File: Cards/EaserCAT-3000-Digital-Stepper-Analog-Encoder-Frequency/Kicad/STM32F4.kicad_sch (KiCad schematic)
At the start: 33 parts, among them J11 5V Power IN, J15 Serial usart1, J17 STLINK, U7 AMS1117-3.3, Y1 8 MHz

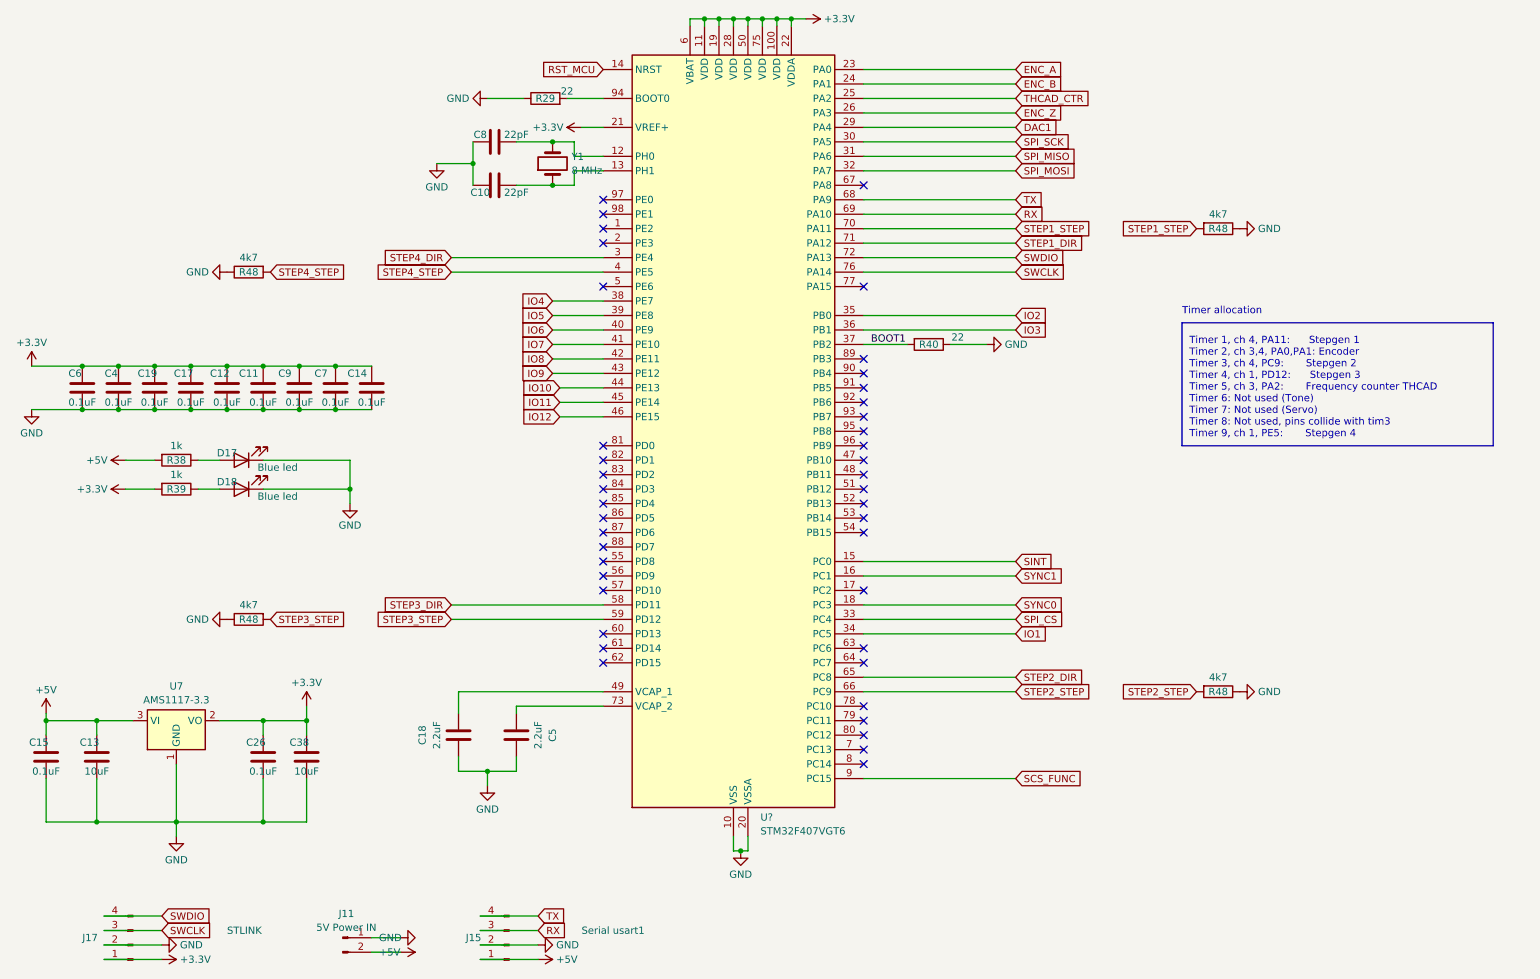
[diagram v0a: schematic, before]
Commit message: Moving all to Kicad8. Housekeeping symbols,libraries,3d-models
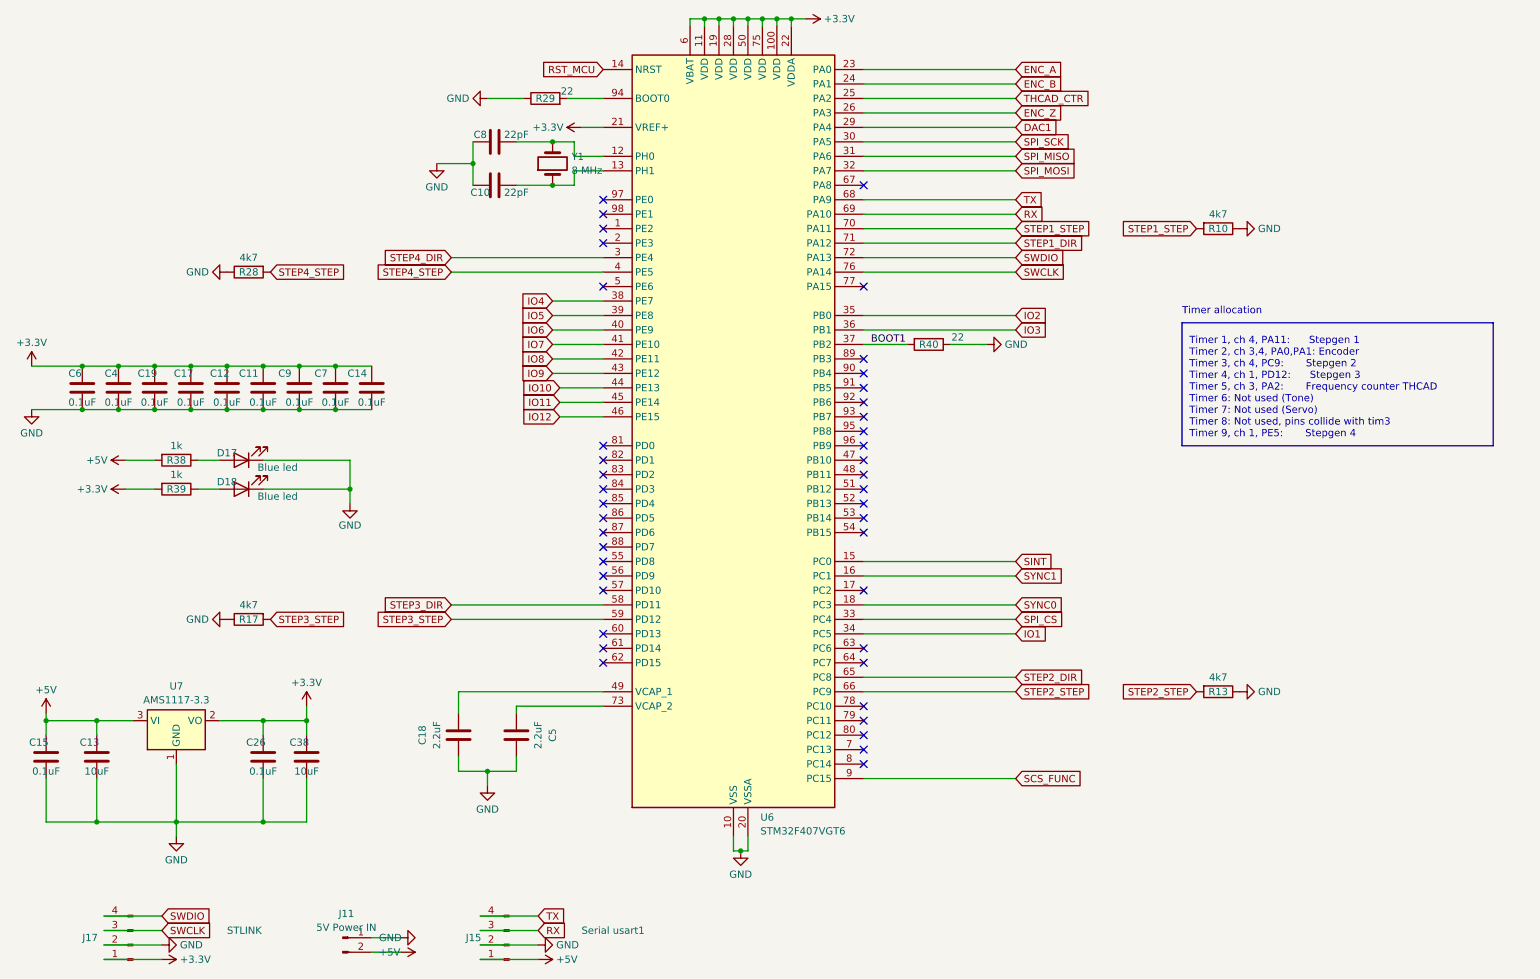
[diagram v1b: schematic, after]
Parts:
- gave numbers to parts that had none: 1
- renumbered R48 to R10, R48 to R13, R48 to R17, R48 to R28

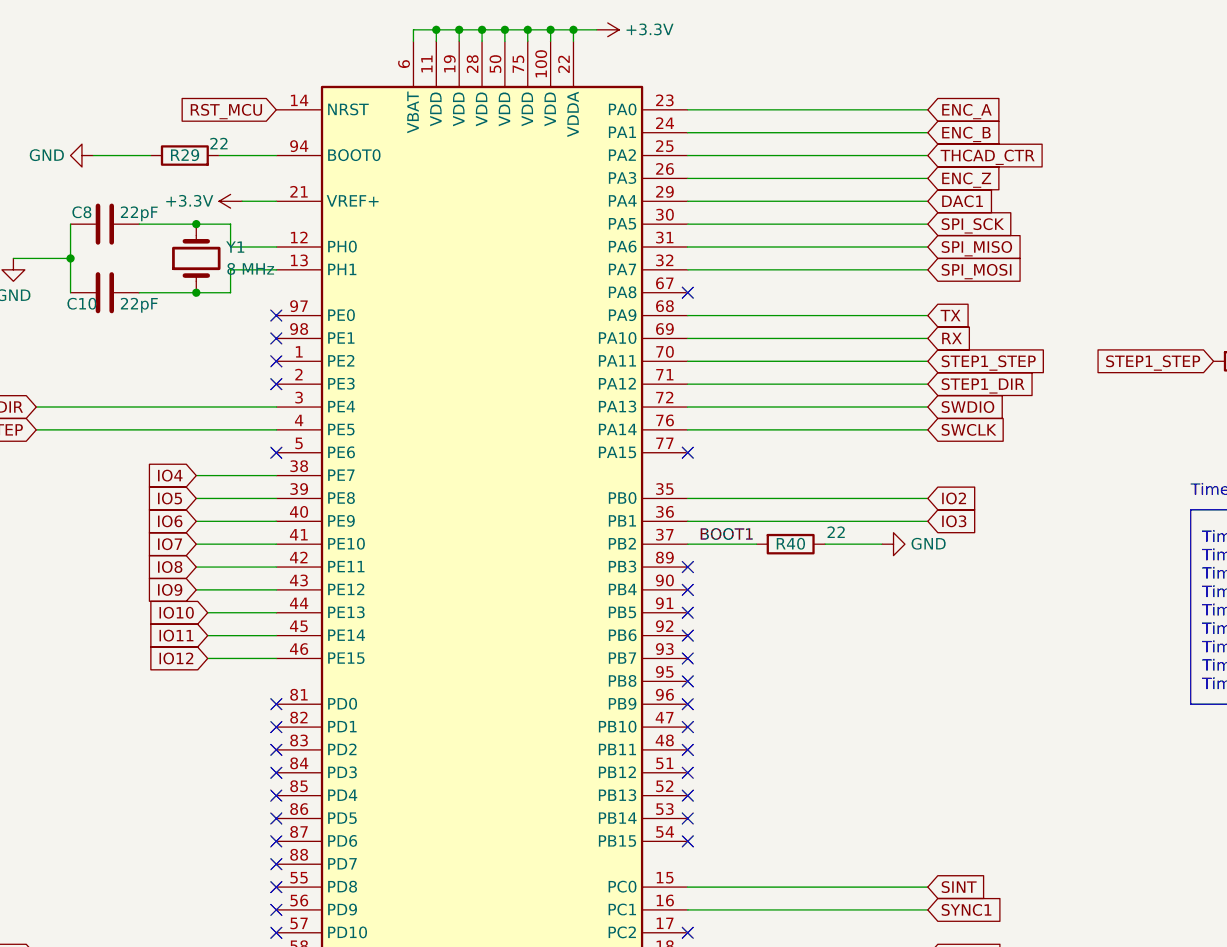
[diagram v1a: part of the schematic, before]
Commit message: Updated reset circuit to PB12
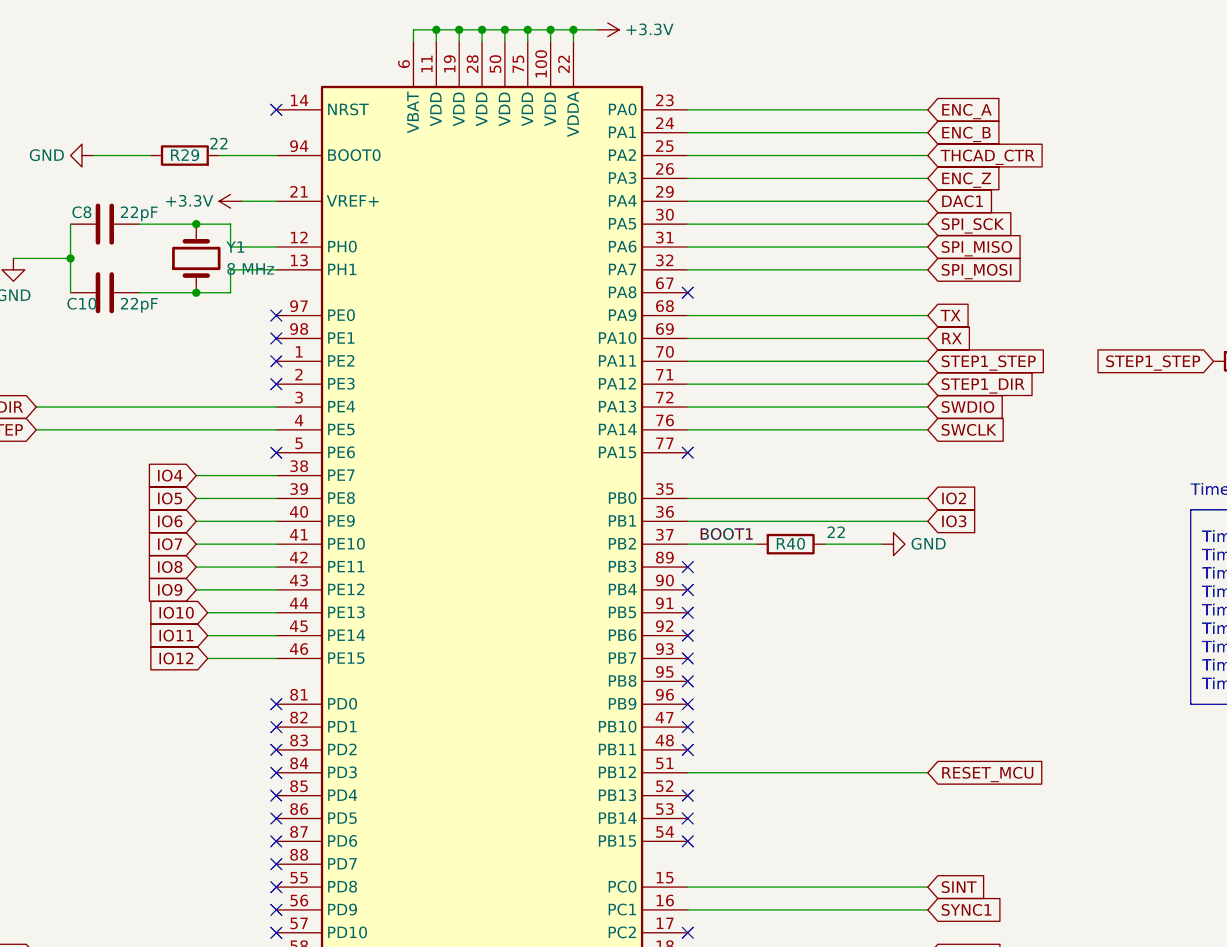
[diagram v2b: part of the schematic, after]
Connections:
- net RESET_MCU: now reaches U6.51 (PB12)
- net RST_MCU: no longer names the net of U6.14 (NRST)
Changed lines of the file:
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@@
-	)
-	(no_connect
-		(at 168.91 100.33)
 	)
 	(no_connect
@@
 	)
 	(no_connect
+		(at 123.19 26.67)
+	)
+	(no_connect
 		(at 123.19 118.11)
 	)
@@
 		(pts
 			(xy 115.57 85.09) (xy 123.19 85.09)
+		)
+		(stroke
+			(width 0)
+			(type default)
+		)
+	)
+	(wire
+		(pts
+			(xy 168.91 100.33) (xy 195.58 100.33)
 		)
 		(stroke
@@
 		)
 	)
-	(global_label "IO6"
-		(shape input)
-		(at 114.3 72.39 180)
-		(fields_autoplaced yes)
-		(effects
-			(font
-				(size 1.27 1.27)
-			)
-			(justify right)
-		)
-		(property "Intersheetrefs" "${INTERSHEET_REFS}"
-			(at 108.17 72.39 0)
+	(global_label "RESET_MCU"
+		(shape input)
+		(at 195.58 100.33 0)
+		(fields_autoplaced yes)
+		(effects
+			(font
+				(size 1.27 1.27)
+			)
+			(justify left)
+		)
+		(property "Intersheetrefs" "${INTERSHEET_REFS}"
+			(at 209.3298 100.33 0)
 			(effects
 				(font
 					(size 1.27 1.27)
 				)
-				(justify right)
+				(justify left)
 				(hide yes)
 			)
 		)
 	)
-	(global_label "RST_MCU"
-		(shape input)
-		(at 123.19 26.67 180)
+	(global_label "IO6"
+		(shape input)
+		(at 114.3 72.39 180)
 		(fields_autoplaced yes)
 		(effects
@@
 		)
 		(property "Intersheetrefs" "${INTERSHEET_REFS}"
-			(at 111.7382 26.67 0)
-			(effects
-				(font
+			(at 108.17 72.39 0)
+			(effects
+				(font
